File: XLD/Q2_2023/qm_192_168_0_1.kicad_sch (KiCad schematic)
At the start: 118 parts, among them T1 Terminator, T10 Terminator, T11 Terminator, T12 Terminator, T13 Terminator, T14 Terminator, T15 Terminator, T16 Terminator, T2 Terminator, T3 Terminator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

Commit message: updating labels
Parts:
- added Splitter28, Splitter29: ZFRSC_183_S+, symbol Quantum Computing:Splitter ZFRSC_183_S+
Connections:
- net QM_1_I9_Q10_OUT: now also Splitter28.
- net QM_1_IN: now also Splitter29.
- net QM_2_I9_Q10_OUT: now also MX23. (RF), OPX2. (LAN), Splitter28.
- net QM_2_IN: now also Splitter29.
- net at Splitter17.: now also Splitter18.; no longer Splitter16.
- net at Splitter15.: now also Splitter13.; no longer Splitter17.
- net at Splitter8.: now also Splitter10.
- net at Splitter6.: now also Splitter5.; no longer Splitter8.
- net at Splitter10.: now also Splitter9.; no longer Splitter8.
- net at Splitter21.: now also Splitter20.
- net at Splitter22.: no longer Splitter21.
- net at Splitter20.: no longer Splitter21.
- net at Splitter13.: now also Splitter12.; no longer Splitter14.
- net at Splitter1.: no longer Splitter2.
- net at Splitter3.: no longer Splitter2.
- net at Splitter4.: now also Splitter3.
- removed net QM_2_10: MX23. (RF), OPX2. (LAN)
- new net: Splitter16., Splitter17.
- new net: Splitter15., Splitter17.
- new net: Splitter6., Splitter8.
- new net: Splitter21., Splitter22.
- new net: Splitter6., Splitter7.
- new net: Splitter13., Splitter14.
- new net: Splitter10., Splitter11.
- new net: Splitter1., Splitter2.
- new net: Splitter2., Splitter3.
- new net QM_OPX1_INPUT: Splitter29.
- new net QM_OPX1_OPX2_OUTPUT: Splitter28.
- now unconnected: Splitter3.
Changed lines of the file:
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@@
     (stroke (width 0) (type default))
   )
-  (wire (pts (xy 247.015 113.538) (xy 255.905 113.538))
-    (stroke (width 0) (type default))
-  )
   (wire (pts (xy 355.6 215.265) (xy 355.6 217.805))
     (stroke (width 0) (type default))
@@
     (stroke (width 0) (type default))
   )
+  (wire (pts (xy 247.015 113.538) (xy 258.826 113.538))
+    (stroke (width 0) (type default))
+  )
   (wire (pts (xy 102.87 267.335) (xy 111.76 267.335))
     (stroke (width 0) (type default))
@@
     (stroke (width 0) (type default))
   )
+  (wire (pts (xy 258.826 113.792) (xy 258.826 113.538))
+    (stroke (width 0) (type default))
+  )
   (wire (pts (xy 374.65 106.045) (xy 328.93 106.045))
     (stroke (width 0) (type default))
@@
     )
   )
-  (global_label "QM_1_I9_Q10_OUT" (shape input) (at 133.858 87.122 0) (fields_autoplaced)
+  (global_label "QM_1_IN" (shape input) (at 106.68 90.17 0) (fields_autoplaced)
     (effects (font (size 1.27 1.27)) (justify left))
-    (property "Intersheetrefs" "${INTERSHEET_REFS}" (at 153.8974 87.122 0)
+    (property "Intersheetrefs" "${INTERSHEET_REFS}" (at 117.5271 90.17 0)
       (effects (font (size 1.27 1.27)) (justify left) hide)
     )
@@
     )
   )
+  (global_label "QM_2_I9_Q10_OUT" (shape input) (at 162.306 150.114 0) (fields_autoplaced)
+    (effects (font (size 1.27 1.27)) (justify left))
+    (property "Intersheetrefs" "${INTERSHEET_REFS}" (at 182.3454 150.114 0)
+      (effects (font (size 1.27 1.27)) (justify left) hide)
+    )
+  )
   (global_label "LO4-SP1" (shape input) (at 375.793 361.823 180) (fields_autoplaced)
     (effects (font (size 1.27 1.27)) (justify right))
@@
     )
   )
+  (global_label "QM_1_IN" (shape input) (at 226.06 148.59 0) (fields_autoplaced)
+    (effects (font (size 1.27 1.27)) (justify left))
+    (property "Intersheetrefs" "${INTERSHEET_REFS}" (at 236.9071 148.59 0)
+      (effects (font (size 1.27 1.27)) (justify left) hide)
+    )
+  )
   (global_label "L03_SP1" (shape output) (at 335.534 303.784 0) (fields_autoplaced)
     (effects (font (size 1.27 1.27)) (justify left))
@@
     )
   )
+  (global_label "QM_2_IN" (shape input) (at 213.36 148.59 180) (fields_autoplaced)
+    (effects (font (size 1.27 1.27)) (justify right))
+    (property "Intersheetrefs" "${INTERSHEET_REFS}" (at 202.5129 148.59 0)
+      (effects (font (size 1.27 1.27)) (justify right) hide)
+    )
+  )
   (global_label "L03-SP1" (shape input) (at 45.085 92.202 180) (fields_autoplaced)
     (effects (font (size 1.27 1.27)) (justify right))
@@
     )
   )
+  (global_label "QM_1_I9_Q10_OUT" (shape input) (at 149.606 150.114 180) (fields_autoplaced)
+    (effects (font (size 1.27 1.27)) (justify right))
+    (property "Intersheetrefs" "${INTERSHEET_REFS}" (at 129.5666 150.114 0)
+      (effects (font (size 1.27 1.27)) (justify right) hide)
+    )
+  )
   (global_label "QM_1_I9_Q10_OUT" (shape output) (at 112.014 108.712 0) (fields_autoplaced)
     (effects (font (size 1.27 1.27)) (justify left))
@@
     )
   )
+  (global_label "QM_2_I9_Q10_OUT" (shape output) (at 258.826 113.792 0) (fields_autoplaced)
+    (effects (font (size 1.27 1.27)) (justify left))
+    (property "Intersheetrefs" "${INTERSHEET_REFS}" (at 278.8654 113.792 0)
+      (effects (font (size 1.27 1.27)) (justify left) hide)
+    )
+  )
+  (global_label "QM_2_IN" (shape input) (at 252.73 95.123 0) (fields_autoplaced)
+    (effects (font (size 1.27 1.27)) (justify left))
+    (property "Intersheetrefs" "${INTERSHEET_REFS}" (at 263.5771 95.123 0)
+      (effects (font (size 1.27 1.27)) (justify left) hide)
+    )
+  )
   (global_label "LO3-SP5" (shape input) (at 344.17 325.755 180) (fields_autoplaced)
     (effects (font (size 1.27 1.27)) (justify right))
@@
     (effects (font (size 1.27 1.27)) (justify left))
   )
+  (hierarchical_label "QM_OPX1_OPX2_OUTPUT" (shape output) (at 155.956 142.494 0) (fields_autoplaced)
+    (effects (font (size 1.27 1.27)) (justify left))
+  )
   (hierarchical_label "QM_4_I5_Q6" (shape input) (at 64.135 229.87 0) (fields_autoplaced)
     (effects (font (size 1.27 1.27)) (justify left))
@@
     (effects (font (size 1.27 1.27)) (justify right))
   )
+  (hierarchical_label "QM_OPX1_INPUT" (shape input) (at 219.71 140.97 0) (fields_autoplaced)
+    (effects (font (size 1.27 1.27)) (justify left))
+  )
   (hierarchical_label "QM_3_3" (shape input) (at 79.375 384.81 270) (fields_autoplaced)
     (effects (font (size 1.27 1.27)) (justify right))
@@
     (effects (font (size 1.27 1.27)) (justify right))
   )
-  (hierarchical_label "QM_1_IN" (shape input) (at 106.68 90.17 0) (fields_autoplaced)
-    (effects (font (size 1.27 1.27)) (justify left))
-  )
   (hierarchical_label "QM_4_I3_Q4" (shape input) (at 64.135 261.747 0) (fields_autoplaced)
     (effects (font (size 1.27 1.27)) (justify left))
   )
-  (hierarchical_label "QM_2_IN" (shape input) (at 252.73 95.25 0) (fields_autoplaced)
-    (effects (font (size 1.27 1.27)) (justify left))
-  )
   (hierarchical_label "QM_8_I3_Q4" (shape input) (at 504.19 111.252 0) (fields_autoplaced)
     (effects (font (size 1.27 1.27)) (justify left))
@@
     (effects (font (size 1.27 1.27)) (justify left))
   )
-  (hierarchical_label "QM_2_I9_Q10_OUT" (shape input) (at 255.905 113.665 0) (fields_autoplaced)
-    (effects (font (size 1.27 1.27)) (justify left))
-  )
   (hierarchical_label "QM_6_I1_Q2" (shape input) (at 360.045 140.97 0) (fields_autoplaced)
     (effects (font (size 1.27 1.27)) (justify left))
@@
     )
   )
+  (symbol (lib_id "Quantum Computing:Splitter ZFRSC_183_S+") (at 219.71 148.59 0) (unit 1)
+    (in_bom yes) (on_board no) (dnp no)
+    (property "Reference" "Splitter29" (at 219.71 153.035 0)
+      (effects (font (size 1.27 1.27)))
+    )
+    (property "Value" "ZFRSC_183_S+" (at 219.71 155.575 0)
+      (effects (font (size 1.27 1.27)))
+    )
+    (property "Footprint" "" (at 219.71 148.59 0)
+      (effects (font (size 1.27 1.27)) hide)
+    )
+    (property "Datasheet" "" (at 219.71 148.59 0)
+      (effects (font (size 1.27 1.27)) hide)
+    )
+    (pin "")
+    (pin "")
+    (pin "")
+    (instances
+      (project "Q2_2023"
+        (path "/9924af8b-9fcb-4325-a1dc-18dd2c4184d7/a7096aa3-4c13-4b44-b9e6-37770984b4aa/c7fee182-06bf-4c41-b3cf-0c2526d9267e"
+          (reference "Splitter29") (unit 1)
+        )
+      )
+    )
+  )
   (symbol (lib_id "Quantum Computing:Mixer IQ Marki") (at 542.925 132.08 0) (mirror x) (unit 1)
     (in_bom yes) (on_board no) (dnp no)
@@
         )
       )
+    )
+  )
+  (symbol (lib_id "Quantum Computing:Splitter ZFRSC_183_S+") (at 155.956 150.114 0) (unit 1)
+    (in_bom yes) (on_board no) (dnp no)
+    (property "Reference" "Splitter28" (at 155.956 154.559 0)
+      (effects (font (size 1.27 1.27)))
+    )
+    (property "Value" "ZFRSC_183_S+" (at 155.956 157.099 0)
+      (effects (font (size 1.27 1.27)))
+    )
+    (property "Footprint" "" (at 155.956 150.114 0)
+      (effects (font (size 1.27 1.27)) hide)
+    )
+    (property "Datasheet" "" (at 155.956 150.114 0)
+      (effects (font (size 1.27 1.27)) hide)
+    )
+    (pin "")
+    (pin "")
+    (pin "")
+    (instances
+      (project "Q2_2023"
+        (path "/9924af8b-9fcb-4325-a1dc-18dd2c4184d7/a7096aa3-4c13-4b44-b9e6-37770984b4aa/c7fee182-06bf-4c41-b3cf-0c2526d9267e"
+          (reference "Splitter28") (unit 1)
+        )
+      )

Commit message: updating labels
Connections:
- net L04-SP1 is gone; now on net QM_1_I1_Q2: MX3. (RF)
- net L04-SP2 is gone; now on net QM_1_I7_Q8: MX7. (RF)
- net L03-SP1: now also MX2. (RF); no longer MX1. (RF)
- net L03-SP2: now also MX3. (RF); no longer MX2. (RF)
- net at Splitter17.: now also Splitter18.; no longer Splitter16.
- net at Splitter15.: now also Splitter13.; no longer Splitter17.
- net at Splitter8.: now also Splitter10.
- net at Splitter6.: now also Splitter5.; no longer Splitter8.
- net at Splitter10.: now also Splitter9.; no longer Splitter8.
- net at Splitter21.: now also Splitter20.
- net at Splitter22.: no longer Splitter21.
- net at Splitter20.: no longer Splitter21.
- net at Splitter13.: now also Splitter12.; no longer Splitter14.
- net at Splitter1.: no longer Splitter2.
- net at Splitter3.: no longer Splitter2.
- net at Splitter4.: now also Splitter3.
- new net: Splitter16., Splitter17.
- new net: Splitter15., Splitter17.
- new net: Splitter6., Splitter8.
- new net: Splitter21., Splitter22.
- new net: Splitter6., Splitter7.
- new net: Splitter13., Splitter14.
- new net: Splitter10., Splitter11.
- new net: Splitter1., Splitter2.
- new net: Splitter2., Splitter3.
- new net L02-SP1: MX1. (RF)
- new net L02-SP2: MX7. (RF)
- now unconnected: Splitter3.
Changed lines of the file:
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@@
     )
   )
-  (global_label "L04-SP1" (shape input) (at 49.657 155.575 180) (fields_autoplaced)
+  (global_label "L03-SP2" (shape input) (at 49.657 155.575 180) (fields_autoplaced)
     (effects (font (size 1.27 1.27)) (justify right))
-    (property "Intersheetrefs" "${INTERSHEET_REFS}" (at 38.0427 155.575 0)
+    (property "Intersheetrefs" "${INTERSHEET_REFS}" (at 37.9633 155.575 0)
       (effects (font (size 1.27 1.27)) (justify right) hide)
     )
@@
     )
   )
-  (global_label "L03-SP1" (shape input) (at 45.085 92.202 180) (fields_autoplaced)
+  (global_label "L02-SP1" (shape input) (at 45.085 92.202 180) (fields_autoplaced)
     (effects (font (size 1.27 1.27)) (justify right))
-    (property "Intersheetrefs" "${INTERSHEET_REFS}" (at 33.4707 92.202 0)
+    (property "Intersheetrefs" "${INTERSHEET_REFS}" (at 33.3913 92.202 0)
       (effects (font (size 1.27 1.27)) (justify right) hide)
     )
@@
     )
   )
-  (global_label "L03-SP2" (shape input) (at 41.275 127.127 180) (fields_autoplaced)
+  (global_label "L03-SP1" (shape input) (at 41.275 127.127 180) (fields_autoplaced)
     (effects (font (size 1.27 1.27)) (justify right))
-    (property "Intersheetrefs" "${INTERSHEET_REFS}" (at 29.6607 127.127 0)
+    (property "Intersheetrefs" "${INTERSHEET_REFS}" (at 29.5813 127.127 0)
       (effects (font (size 1.27 1.27)) (justify right) hide)
     )
   )
-  (global_label "L04-SP2" (shape input) (at 100.965 164.592 180) (fields_autoplaced)
+  (global_label "L02-SP2" (shape input) (at 100.965 164.592 180) (fields_autoplaced)
     (effects (font (size 1.27 1.27)) (justify right))
-    (property "Intersheetrefs" "${INTERSHEET_REFS}" (at 89.3507 164.592 0)
+    (property "Intersheetrefs" "${INTERSHEET_REFS}" (at 89.2713 164.592 0)
       (effects (font (size 1.27 1.27)) (justify right) hide)
     )

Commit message: updatede de line B 5 qubits
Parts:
- removed Splitter10, Splitter11, Splitter12, Splitter13, Splitter14, Splitter15, Splitter16, Splitter17, Splitter18, Splitter25, Splitter5, Splitter6, Splitter7, Splitter8, Splitter9: ZFRSC_183_S+, symbol Quantum Computing:Splitter ZFRSC_183_S+
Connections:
- net LO6-SP1 is gone; now on net QM_2_IN: MX20. (RF)
- net LO6-SP2 is gone; now on net QM_2_I9_Q10_OUT: MX23. (RF)
- net LO4-SP1: now also MX20. (RF)
- net LO4-SP2: now also MX23. (RF)
- net L0-06: now reaches LO16.
- net at Splitter21.: now also Splitter20.
- net at Splitter22.: no longer Splitter21.
- net at Splitter20.: no longer Splitter21.
- net at Splitter1.: no longer Splitter2.
- net at Splitter3.: no longer Splitter2.
- net at Splitter4.: now also Splitter3.
- net QM_OPX1_INPUT renamed QM_OPX1_OPX2_INPUT
- new net: Splitter21., Splitter22.
- new net: Splitter1., Splitter2.
- new net: Splitter2., Splitter3.
- now unconnected: Splitter3.
- no-connect marks 27 -> 19
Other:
- moved on the sheet: LO11, LO12, LO13, LO14, LO16, LO4, Splitter23, Splitter24, Splitter26, Splitter27

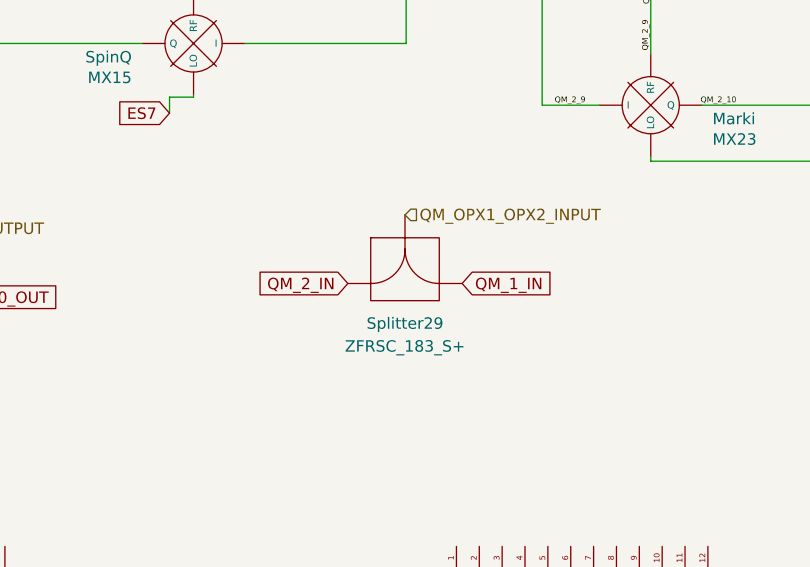
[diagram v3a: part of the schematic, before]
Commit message: correct tag type for input in opx1 and opx2
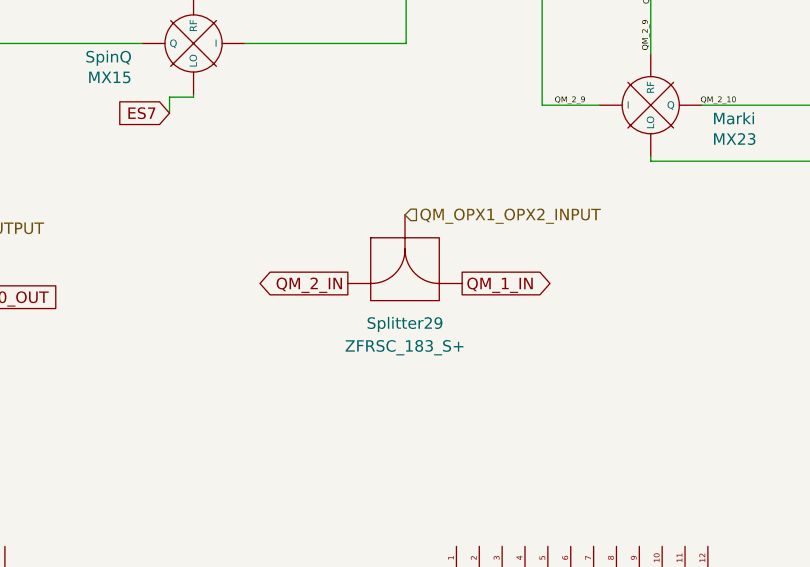
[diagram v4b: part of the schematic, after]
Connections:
- net at Splitter21.: now also Splitter20.
- net at Splitter22.: no longer Splitter21.
- net at Splitter20.: no longer Splitter21.
- net at Splitter1.: no longer Splitter2.
- net at Splitter3.: no longer Splitter2.
- net at Splitter4.: now also Splitter3.
- new net: Splitter21., Splitter22.
- new net: Splitter1., Splitter2.
- new net: Splitter2., Splitter3.
- now unconnected: Splitter3.
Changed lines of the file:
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@@
     )
   )
-  (global_label "QM_1_IN" (shape input) (at 226.06 148.59 0) (fields_autoplaced)
+  (global_label "QM_1_IN" (shape output) (at 226.06 148.59 0) (fields_autoplaced)
     (effects (font (size 1.27 1.27)) (justify left))
-    (property "Intersheetrefs" "${INTERSHEET_REFS}" (at 236.9071 148.59 0)
+    (property "Intersheetrefs" "${INTERSHEET_REFS}" (at 236.8277 148.59 0)
       (effects (font (size 1.27 1.27)) (justify left) hide)
     )
@@
     )
   )
-  (global_label "QM_2_IN" (shape input) (at 213.36 148.59 180) (fields_autoplaced)
+  (global_label "QM_2_IN" (shape output) (at 213.36 148.59 180) (fields_autoplaced)
     (effects (font (size 1.27 1.27)) (justify right))
-    (property "Intersheetrefs" "${INTERSHEET_REFS}" (at 202.5129 148.59 0)
+    (property "Intersheetrefs" "${INTERSHEET_REFS}" (at 202.5923 148.59 0)
       (effects (font (size 1.27 1.27)) (justify right) hide)
     )
